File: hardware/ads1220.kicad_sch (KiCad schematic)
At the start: 39 parts, among them J1 Conn_01x04_Female, J2 Conn_01x04_Female, U1 LM4140-1.25, U2 MIC5205-2.5YM5, U3 ADS1220

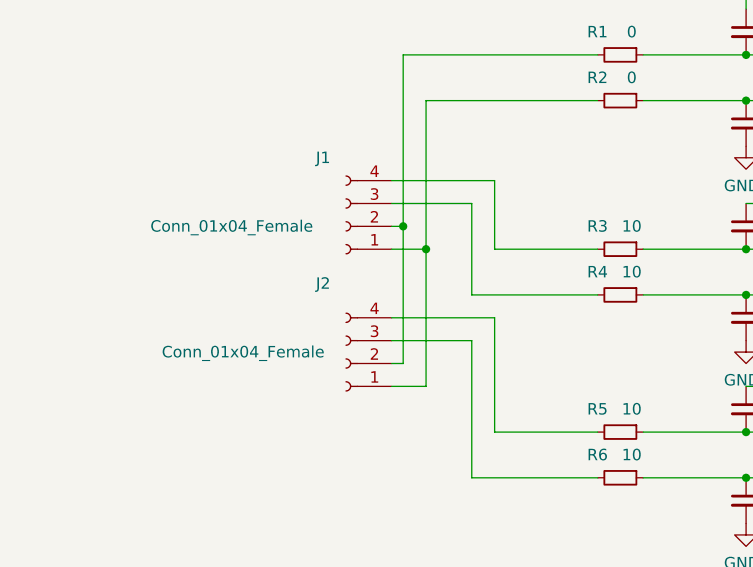
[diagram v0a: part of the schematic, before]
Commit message: datasheets and PCB mod to molex-minifit connector
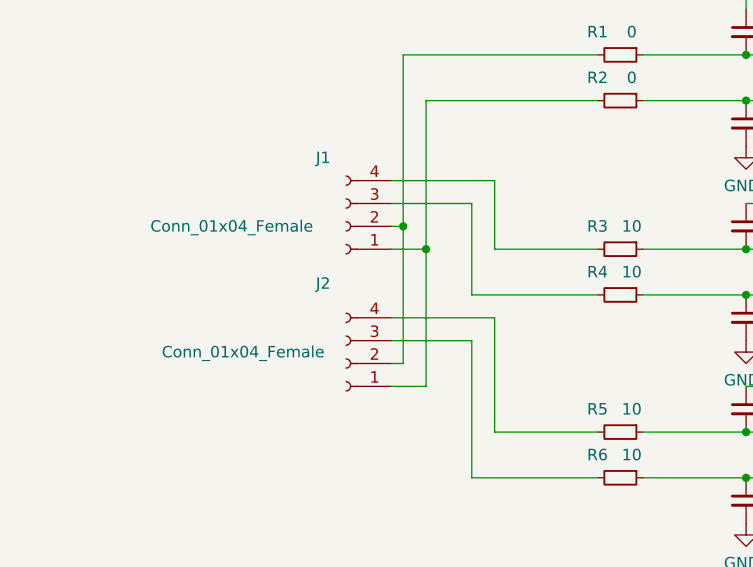
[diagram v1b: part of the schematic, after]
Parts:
- J1, J2: footprint (none) -> Connector_Molex:Molex_Nano-Fit_105314-xx04_2x02_P2.50mm_Horizontal

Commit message: hardware updates
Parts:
- C1, C10, C11, C12, C13, C14, C15, C2, C3, C4, C5, C6, C7, C8, C9: footprint (none) -> Capacitor_SMD:C_0805_2012Metric_Pad1.18x1.45mm_HandSolder
- R1, R10, R11, R13, R14, R2, R3, R4, R5, R6, R7, R8: footprint (none) -> Resistor_SMD:R_0805_2012Metric_Pad1.20x1.40mm_HandSolder
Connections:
- net at R4.2: now also J1.2 (Pin_2); no longer J1.3 (Pin_3)
- net at R3.2: now also J1.1 (Pin_1); no longer J1.4 (Pin_4)
- net at R6.2: now also J2.2 (Pin_2); no longer J2.3 (Pin_3)
- net at R5.2: now also J2.1 (Pin_1); no longer J2.4 (Pin_4)
- new net: J1.4 (Pin_4), J2.4 (Pin_4), R2.2
- new net: J1.3 (Pin_3), J2.3 (Pin_3), R1.2
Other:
- moved on the sheet: J1, J2
